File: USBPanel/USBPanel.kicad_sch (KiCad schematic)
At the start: 66 parts, among them J1 PORT1, J2 PORT2, J3 PWR, J4 USB_UFP, J5 SINK, J6 I2Ct, J7 I2Cc, Q1 ISZ0702NLS, Q2 ISZ0702NLS, Q3 NX138BK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

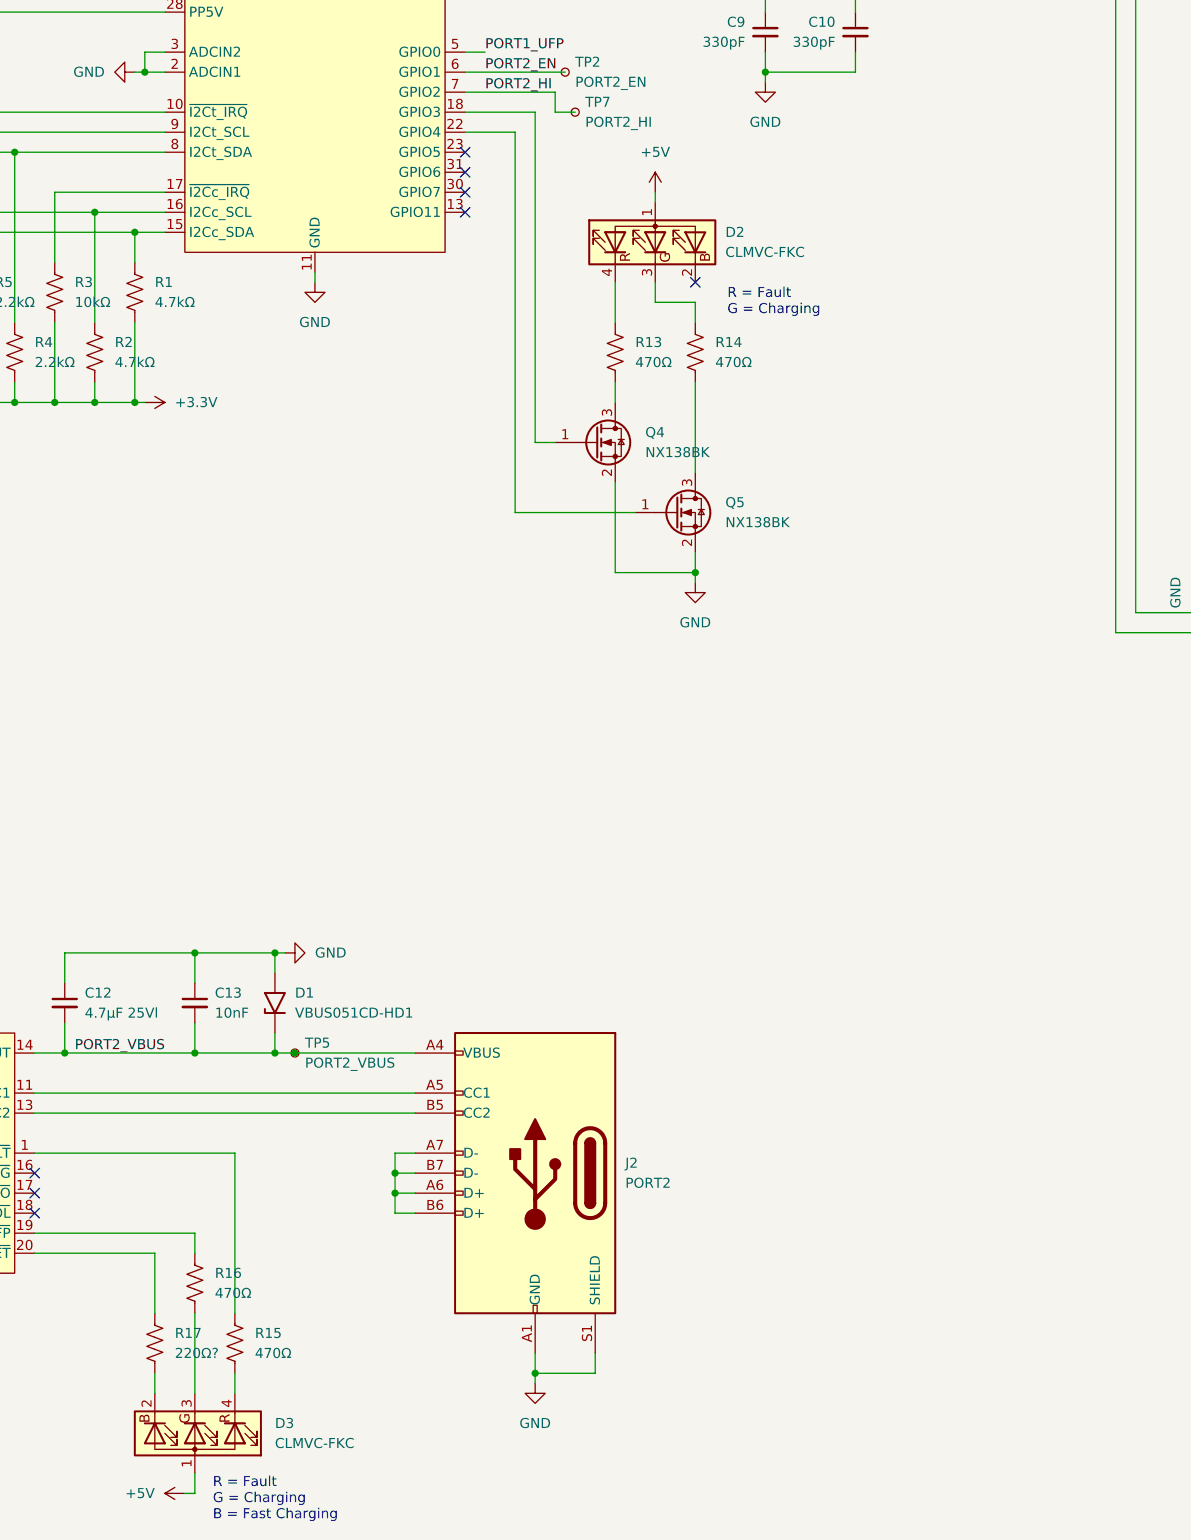
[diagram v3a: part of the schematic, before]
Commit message: USBPanel configuration and post-build edits
Changed LED colour assignments and resistor values.
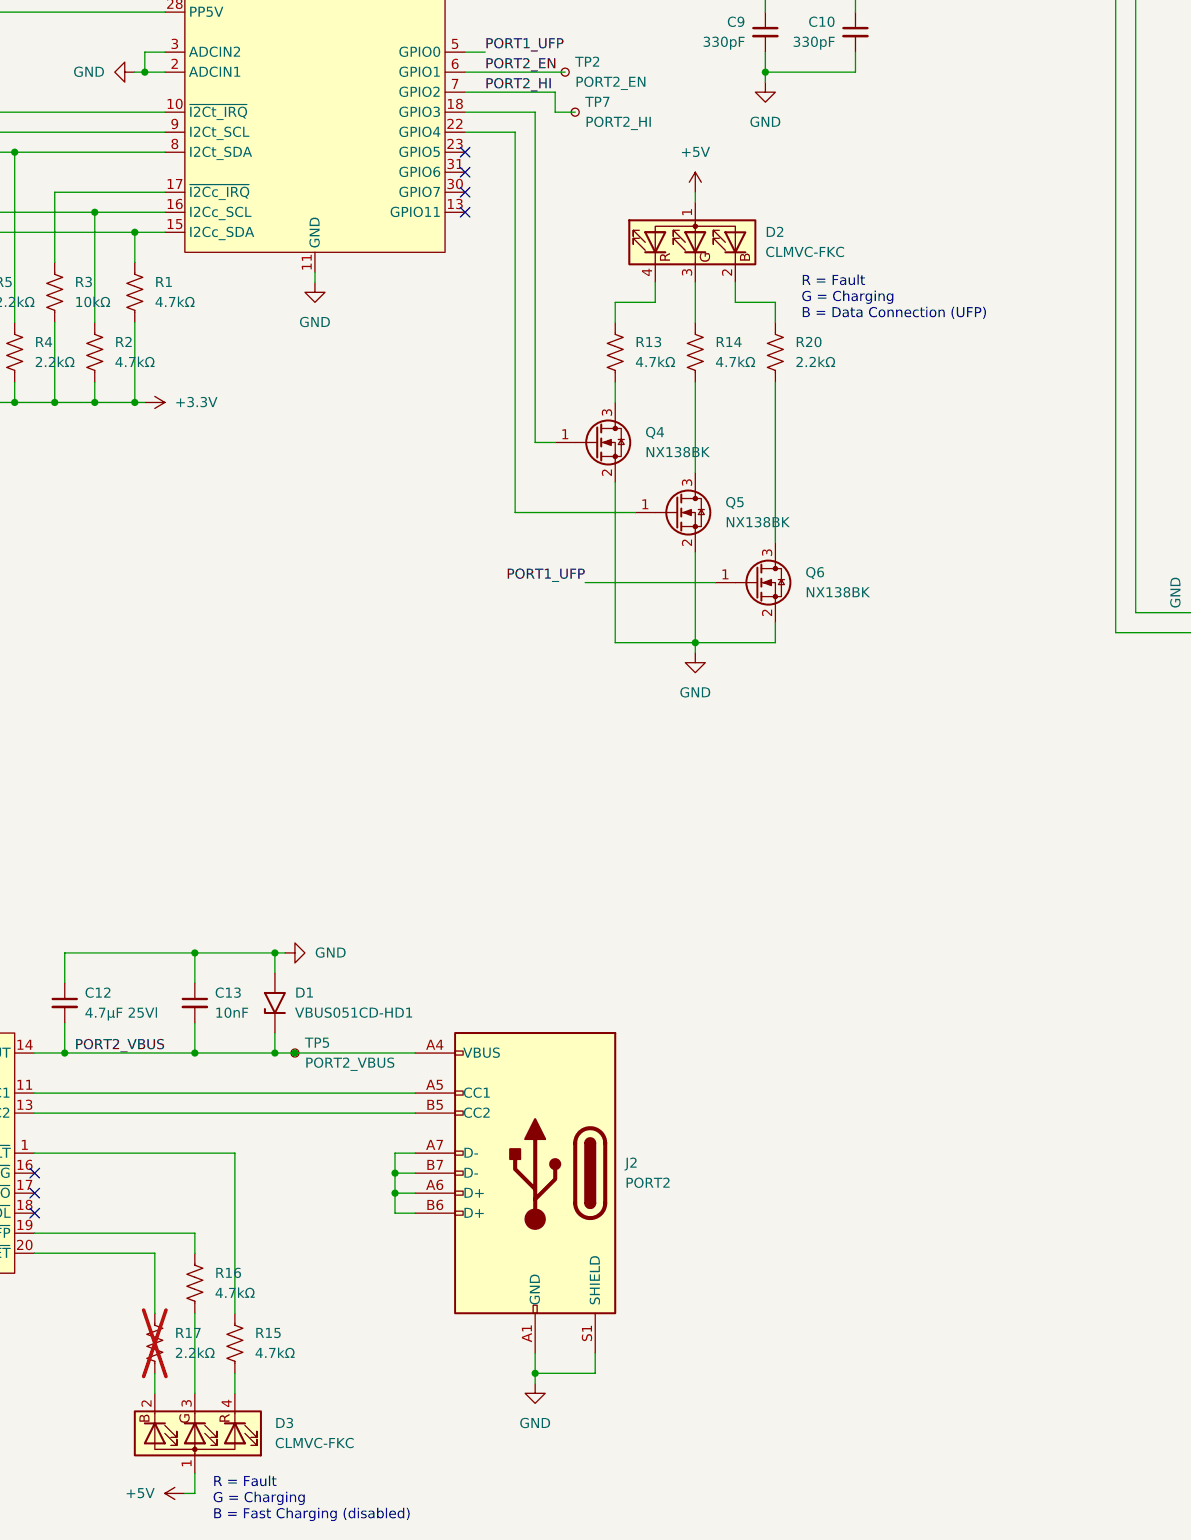
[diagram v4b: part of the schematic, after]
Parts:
- added Q6: NX138BK, Package_TO_SOT_SMD:SOT-23, symbol Transistor_FET:Q_NMOS_GSD
- added R20: 2.2kΩ, Resistor_SMD:R_0603_1608Metric, symbol Device:R_US
- R13, R14, R15, R16: value 470Ω -> 4.7kΩ
- R17: value 220Ω? -> 2.2kΩ; now not fitted
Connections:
- net GND: now also Q6.2 (S)
- net PORT1_UFP: now also Q6.1 (G)
- net at D2.2 (BK): now also R20.1
- new net: Q6.3 (D), R20.2
- no-connect marks 10 -> 9
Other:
- note added: "R = Fault G = Charging B = Data Connection (UFP)"
- note added: "R = Fault G = Charging B = Fast Charging (disabled)"
- note removed: "R = Fault G = Charging"
- note removed: "R = Fault G = Charging B = Fast Charging"
- moved on the sheet: D2
